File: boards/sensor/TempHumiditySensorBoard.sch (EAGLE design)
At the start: 6 parts

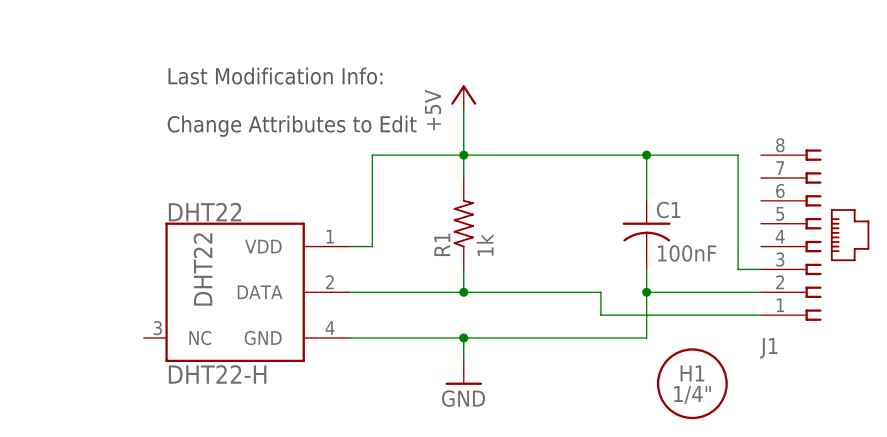
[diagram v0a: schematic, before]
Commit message: QR Code appears on schematic, has 'QR' identifier
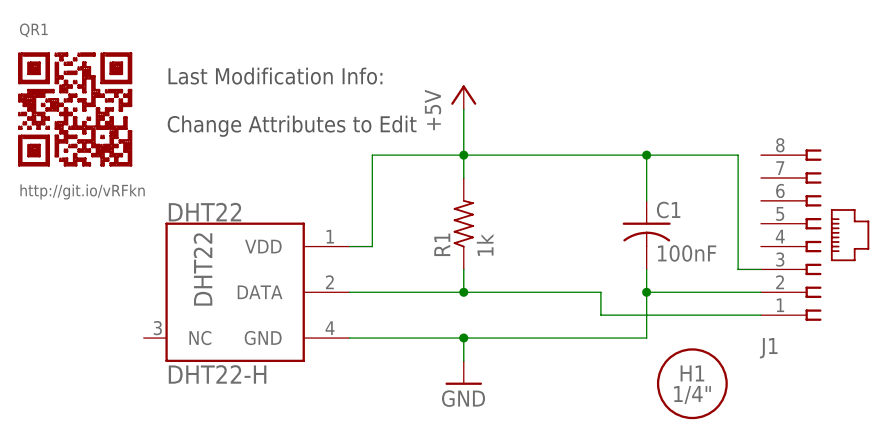
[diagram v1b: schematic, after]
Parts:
- added QR1: QR-HTTP://GIT.IO/VRFKN, QR-git.io-vRFkn:QR-HTTP://GIT.IO/VRFKN
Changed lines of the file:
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@@
 </part>
 <part name="H1" library="JQI-holes" deviceset="MOUNT-HOLE" device="-1/4&quot;-FREE"/>
+<part name="QR1" library="QR-git.io-vRFkn" deviceset="QR-HTTP://GIT.IO/VRFKN" device=""/>
 </parts>
 <sheets>
@@
 </instance>
 <instance part="H1" gate="G$1" x="60.96" y="2.54"/>
+<instance part="QR1" gate="G$1" x="-7.62" y="33.02"/>
 </instances>
 <busses>

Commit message: MacroFab files and BOM
Added BOMs for use with eagle-config and production files for MacroFab.

DSB
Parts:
- C1: PARTNO (none) -> CL31B104JBCNNNC
- DHT22: PARTNO (none) -> 385
- J1: PARTNO (none) -> 555164-1
- R1: PARTNO (none) -> ERJ-8ENF2001V
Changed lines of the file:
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@@
 <?xml version="1.0" encoding="utf-8"?>
 <!DOCTYPE eagle SYSTEM "eagle.dtd">
-<eagle version="6.6.0">
+<eagle version="8.5.0">
 <drawing>
 <settings>
 <setting alwaysvectorfont="no"/>
+<setting keepoldvectorfont="yes"/>
 <setting verticaltext="up"/>
 </settings>
-<grid distance="0.1" unitdist="inch" unit="inch" style="lines" multiple="1" display="no" altdistance="0.01" altunitdist="inch" altunit="inch"/>
+<grid distance="0.05" unitdist="inch" unit="inch" style="lines" multiple="1" display="no" altdistance="0.01" altunitdist="inch" altunit="inch"/>
 <layers>
 <layer number="1" name="Top" color="4" fill="1" visible="no" active="no"/>
@@
 </classes>
 <parts>
-<part name="DHT22" library="dht22" deviceset="DHT22" device="-H"/>
+<part name="DHT22" library="dht22" deviceset="DHT22" device="-H">
+<attribute name="PARTNO" value="385"/>
+</part>
 <part name="P+1" library="supply1" deviceset="+5V" device=""/>
 <part name="GND1" library="supply1" deviceset="GND" device=""/>
-<part name="J1" library="con-amp" deviceset="555164-1" device=""/>
-<part name="C1" library="resistor" deviceset="C-US" device="C1206" value="100nF"/>
-<part name="R1" library="resistor" deviceset="R-US_" device="R1206" value="1k"/>
+<part name="J1" library="con-amp" deviceset="555164-1" device="">
+<attribute name="PARTNO" value="555164-1"/>
+</part>
+<part name="C1" library="resistor" deviceset="C-US" device="C1206" value="100nF">
+<attribute name="PARTNO" value="CL31B104JBCNNNC"/>
+</part>
+<part name="R1" library="resistor" deviceset="R-US_" device="R1206" value="1k">
+<attribute name="PARTNO" value="ERJ-8ENF2001V"/>
+</part>
 <part name="U$2" library="info" deviceset="INFO" device="ROW">
 <attribute name="MODAUTH" value="ZSS"/>
@@
 </plain>
 <instances>
-<instance part="DHT22" gate="G$1" x="17.78" y="12.7"/>
+<instance part="DHT22" gate="G$1" x="17.78" y="12.7">
+<attribute name="PARTNO" x="17.78" y="12.7" size="1.778" layer="96" display="off"/>
+</instance>
 <instance part="P+1" gate="1" x="35.56" y="35.56"/>
 <instance part="GND1" gate="1" x="35.56" y="2.54"/>
-<instance part="J1" gate="G$1" x="73.66" y="17.78" rot="MR180"/>
-<instance part="C1" gate="G$1" x="55.88" y="20.32"/>
-<instance part="R1" gate="G$1" x="35.56" y="20.32" rot="R90"/>
+<instance part="J1" gate="G$1" x="73.66" y="17.78" rot="MR180">
+<attribute name="PARTNO" x="73.66" y="17.78" size="1.778" layer="96" display="off"/>
+</instance>
+<instance part="C1" gate="G$1" x="55.88" y="20.32">
+<attribute name="PARTNO" x="55.88" y="20.32" size="1.778" layer="96" display="off"/>
+</instance>
+<instance part="R1" gate="G$1" x="35.56" y="20.32" rot="R90">
+<attribute name="PARTNO" x="35.56" y="20.32" size="1.778" layer="96" display="off"/>
+</instance>
 <instance part="U$2" gate="G$1" x="2.54" y="30.48">
 <attribute name="MODAUTH" x="2.54" y="30.48" size="1.778" layer="96" display="off"/>
